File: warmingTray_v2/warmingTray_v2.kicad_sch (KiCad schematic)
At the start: 37 parts, among them J1 Jack-DC, P1 Power, P2 Analog, P3 Analog, P4 Digital, P5 PWM, P6 PWM, P7 Communication

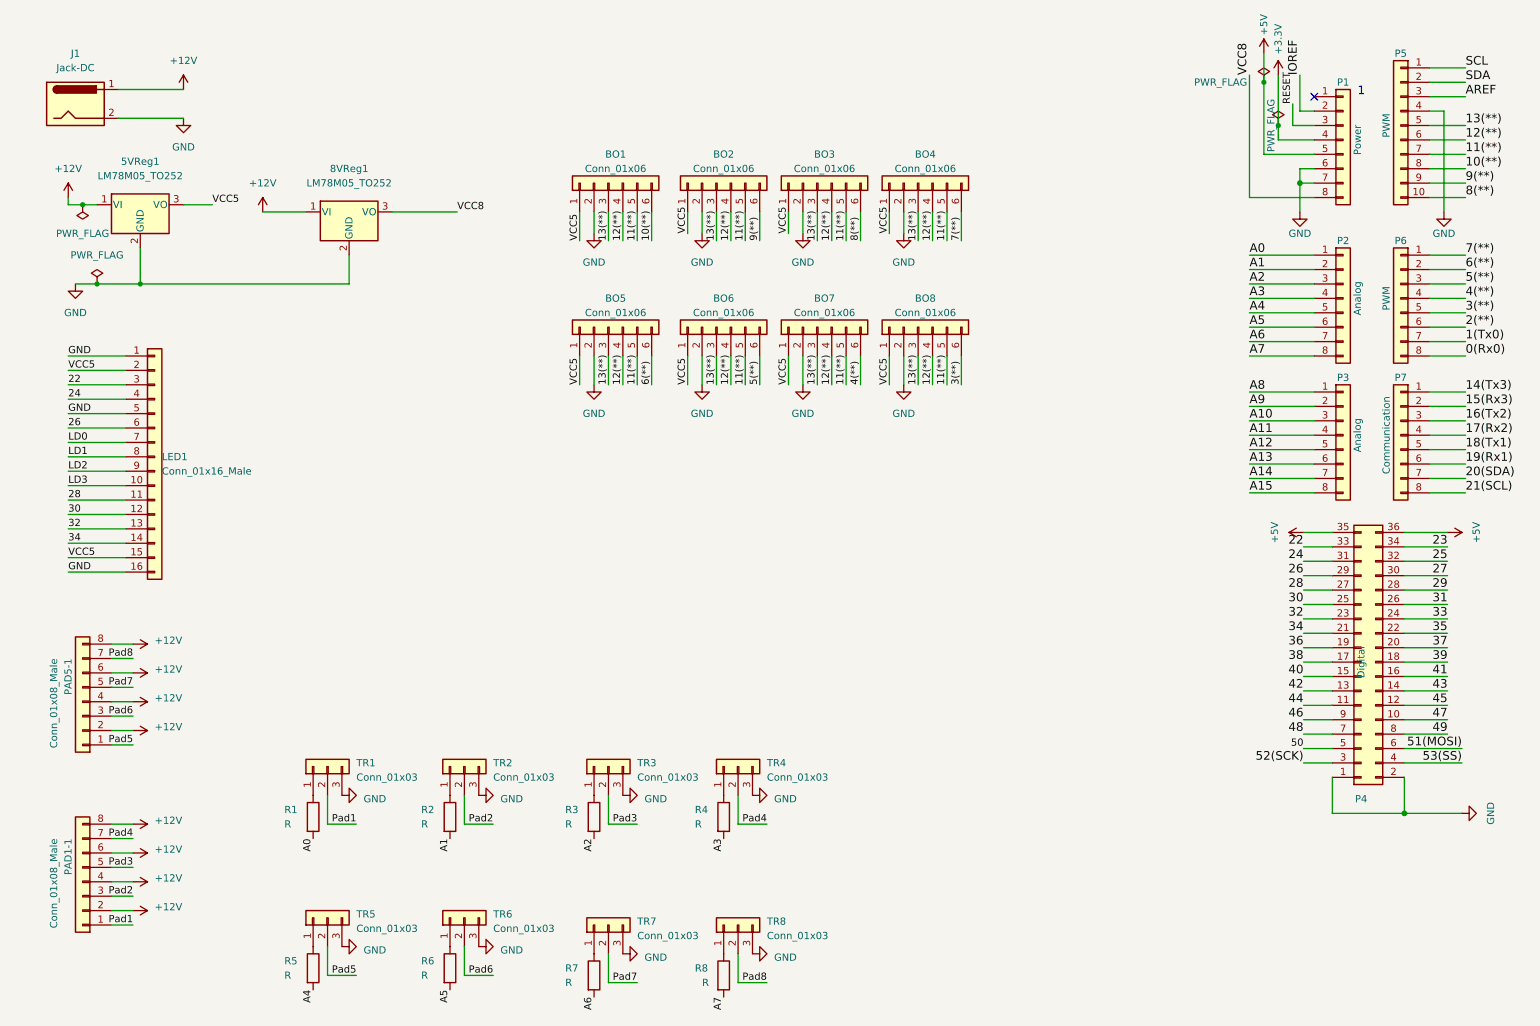
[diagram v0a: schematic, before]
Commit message: added traces to pcb
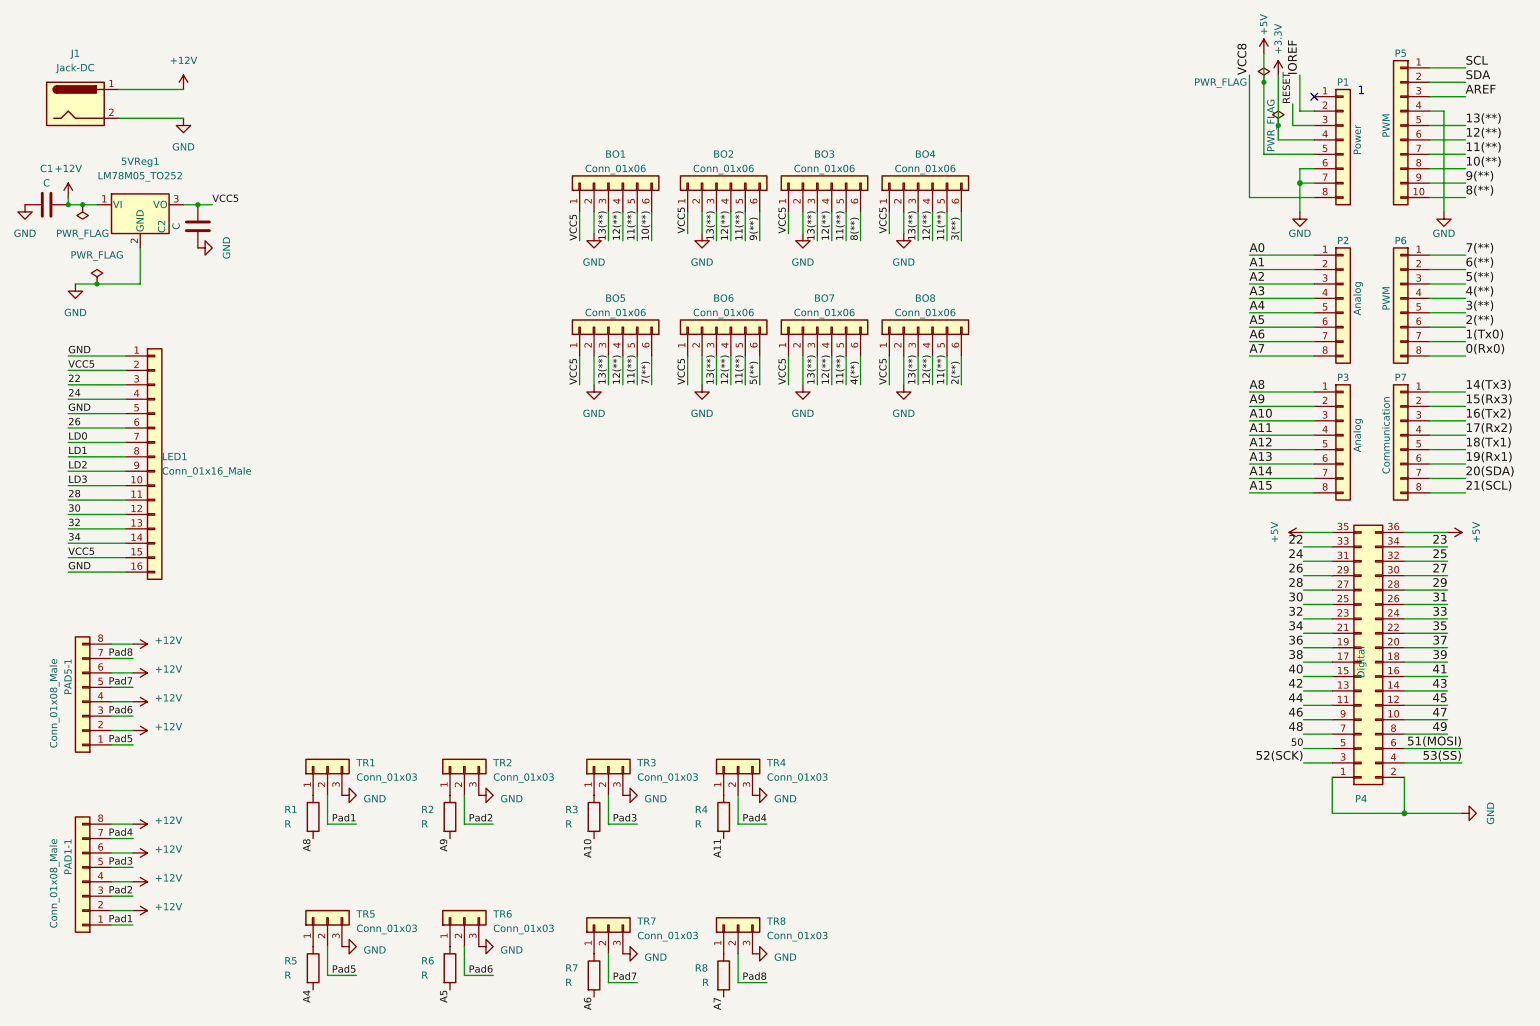
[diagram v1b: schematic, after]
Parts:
- removed 8VReg1: LM78M05_TO252, Package_TO_SOT_SMD:TO-252-2, symbol Regulator_Linear:LM78M05_TO252
- added C1: C, footprints_0-33uF:CAP_1608_TDK, symbol Device:C
- added C2: C, footprints_0-1uF_Capacitor:CAP_CL05_SAM, symbol Device:C
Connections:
- net +12V: now also C1.2
- net 2(**): now also BO8.6 (Pin_6)
- net 3(**): now also BO4.6 (Pin_6); no longer BO8.6 (Pin_6)
- net 6(**): no longer BO5.6 (Pin_6)
- net 7(**): now also BO5.6 (Pin_6); no longer BO4.6 (Pin_6)
- net A0: no longer R1.2
- net A1: no longer R2.2
- net A10: now also R3.2
- net A11: now also R4.2
- net A2: no longer R3.2
- net A3: no longer R4.2
- net A8: now also R1.2
- net A9: now also R2.2
- net GND: now also C1.1, C2.1
- net VCC5: now also C2.2
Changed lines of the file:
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@@
   (junction (at 240.03 43.18) (diameter 1.016) (color 0 0 0 0)
   )
-  (junction (at 35.56 60.96) (diameter 0) (color 0 0 0 0)
-  )
   (junction (at 25.4 46.99) (diameter 0) (color 0 0 0 0)
   )
@@
   (junction (at 258.445 154.305) (diameter 1.016) (color 0 0 0 0)
   )
+  (junction (at 22.86 46.99) (diameter 0) (color 0 0 0 0)
+  )
+  (junction (at 45.72 46.99) (diameter 0) (color 0 0 0 0)
+  )
   (junction (at 236.22 33.02) (diameter 0) (color 0 0 0 0)
   )
@@
     (stroke (width 0) (type solid))
   )
-  (wire (pts (xy 80.01 48.26) (xy 91.44 48.26))
-    (stroke (width 0) (type default))
-  )
   (wire (pts (xy 152.4 73.66) (xy 152.4 78.74))
     (stroke (width 0) (type default))
@@
     (stroke (width 0) (type solid))
   )
-  (wire (pts (xy 43.18 46.99) (xy 48.26 46.99))
+  (wire (pts (xy 43.18 46.99) (xy 45.72 46.99))
     (stroke (width 0) (type default))
   )
@@
     (stroke (width 0) (type solid))
   )
+  (wire (pts (xy 45.72 46.99) (xy 48.26 46.99))
+    (stroke (width 0) (type default))
+  )
   (wire (pts (xy 231.14 63.5) (xy 242.57 63.5))
     (stroke (width 0) (type solid))
@@
     (stroke (width 0) (type default))
   )
-  (wire (pts (xy 57.15 48.26) (xy 64.77 48.26))
-    (stroke (width 0) (type default))
-  )
   (wire (pts (xy 240.03 40.64) (xy 240.03 43.18))
     (stroke (width 0) (type solid))
@@
     (stroke (width 0) (type default))
   )
-  (wire (pts (xy 72.39 60.96) (xy 35.56 60.96))
-    (stroke (width 0) (type default))
-  )
   (wire (pts (xy 238.76 29.21) (xy 238.76 33.02))
     (stroke (width 0) (type default))
@@
     (stroke (width 0) (type solid))
   )
-  (wire (pts (xy 72.39 55.88) (xy 72.39 60.96))
-    (stroke (width 0) (type default))
-  )
   (wire (pts (xy 154.94 48.26) (xy 154.94 53.34))
     (stroke (width 0) (type default))
@@
     (effects (font (size 1.524 1.524)) (justify left bottom))
   )
-  (label "6(**)" (at 125.73 78.74 90) (fields_autoplaced)
+  (label "7(**)" (at 125.73 78.74 90) (fields_autoplaced)
     (effects (font (size 1.27 1.27)) (justify left bottom))
   )
@@
     (effects (font (size 1.524 1.524)) (justify right bottom))
   )
-  (label "3(**)" (at 180.34 78.74 90) (fields_autoplaced)
+  (label "2(**)" (at 180.34 78.74 90) (fields_autoplaced)
     (effects (font (size 1.27 1.27)) (justify left bottom))
   )
@@
     (effects (font (size 1.524 1.524)) (justify right bottom))
   )
-  (label "A0" (at 66.04 158.75 270) (fields_autoplaced)
+  (label "A8" (at 66.04 158.75 270) (fields_autoplaced)
     (effects (font (size 1.27 1.27)) (justify right bottom))
   )
@@
     (effects (font (size 1.27 1.27)) (justify right bottom))
   )
-  (label "7(**)" (at 180.34 53.34 90) (fields_autoplaced)
+  (label "3(**)" (at 180.34 53.34 90) (fields_autoplaced)
     (effects (font (size 1.27 1.27)) (justify left bottom))
   )
@@
     (effects (font (size 1.524 1.524)) (justify right bottom))
   )
-  (label "A1" (at 90.17 158.75 270) (fields_autoplaced)
+  (label "A9" (at 90.17 158.75 270) (fields_autoplaced)
     (effects (font (size 1.27 1.27)) (justify right bottom))
   )
@@
     (effects (font (size 1.524 1.524)) (justify left bottom))
   )
-  (label "A2" (at 115.57 158.75 270) (fields_autoplaced)
+  (label "A10" (at 115.57 158.75 270) (fields_autoplaced)
     (effects (font (size 1.27 1.27)) (justify right bottom))
   )
@@
     (effects (font (size 1.27 1.27)) (justify right bottom))
   )
-  (label "A3" (at 138.43 158.75 270) (fields_autoplaced)
+  (label "A11" (at 138.43 158.75 270) (fields_autoplaced)
     (effects (font (size 1.27 1.27)) (justify right bottom))
   )
@@
     (effects (font (size 1.27 1.27)) (justify left bottom))
   )
-  (label "VCC8" (at 91.44 48.26 0) (fields_autoplaced)
-    (effects (font (size 1.27 1.27)) (justify left bottom))
-  )
   (label "Pad3" (at 123.19 156.21 180) (fields_autoplaced)
     (effects (font (size 1.27 1.27)) (justify right bottom))
@@
     )
   )
+  (symbol (lib_id "Device:C") (at 19.05 46.99 90) (unit 1)
+    (in_bom yes) (on_board yes) (dnp no) (fields_autoplaced)
+    (property "Reference" "C1" (at 19.05 40.64 90)
+      (effects (font (size 1.27 1.27)))
+    )
+    (property "Value" "C" (at 19.05 43.18 90)
+      (effects (font (size 1.27 1.27)))
+    )
+    (property "Footprint" "footprints_0-33uF:CAP_1608_TDK" (at 22.86 46.0248 0)
+      (effects (font (size 1.27 1.27)) hide)
+    )
+    (property "Datasheet" "~" (at 19.05 46.99 0)
+      (effects (font (size 1.27 1.27)) hide)
+    )
+    (pin "1")
+    (pin "2")
+    (instances
+      (project "warmingTray_v2"
+        (path "/3761374c-22ef-4655-8f2e-3ccb2e58d193"
+          (reference "C1") (unit 1)
+        )
+      )
+    )
+  )
   (symbol (lib_id "Connector_Generic:Conn_01x08") (at 257.81 63.5 0) (mirror y) (unit 1)
     (in_bom yes) (on_board yes) (dnp no)
@@
     )
   )
+  (symbol (lib_id "Device:C") (at 45.72 50.8 180) (unit 1)
+    (in_bom yes) (on_board yes) (dnp no) (fields_autoplaced)
+    (property "Reference" "C2" (at 39.37 50.8 90)
+      (effects (font (size 1.27 1.27)))
+    )
+    (property "Value" "C" (at 41.91 50.8 90)
+      (effects (font (size 1.27 1.27)))
+    )
+    (property "Footprint" "footprints_0-1uF_Capacitor:CAP_CL05_SAM" (at 44.7548 46.99 0)
+      (effects (font (size 1.27 1.27)) hide)
+    )
+    (property "Datasheet" "~" (at 45.72 50.8 0)
+      (effects (font (size 1.27 1.27)) hide)
+    )
+    (pin "1")
+    (pin "2")
+    (instances
+      (project "warmingTray_v2"
+        (path "/3761374c-22ef-4655-8f2e-3ccb2e58d193"
+          (reference "C2") (unit 1)
+        )
+      )
+    )
+  )
   (symbol (lib_id "Connector_Generic:Conn_01x03") (at 118.11 173.99 90) (unit 1)
     (in_bom yes) (on_board yes) (dnp no) (fields_autoplaced)
@@
     )
   )
-  (symbol (lib_id "power:+12V") (at 57.15 48.26 0) (unit 1)
-    (in_bom yes) (on_board yes) (dnp no) (fields_autoplaced)
-    (property "Reference" "#PWR0117" (at 57.15 52.07 0)
-      (effects (font (size 1.27 1.27)) hide)
-    )
-    (property "Value" "+12V" (at 57.15 43.18 0)
-      (effects (font (size 1.27 1.27)))
-    )
-    (property "Footprint" "" (at 57.15 48.26 0)
-      (effects (font (size 1.27 1.27)) hide)
-    )
-    (property "Datasheet" "" (at 57.15 48.26 0)
-      (effects (font (size 1.27 1.27)) hide)
-    )
-    (pin "1")
-    (instances
-      (project "warmingTray_v2"
-        (path "/3761374c-22ef-4655-8f2e-3ccb2e58d193"
-          (reference "#PWR0117") (unit 1)
-        )
-      )
-    )
-  )
   (symbol (lib_id "Connector_Generic:Conn_01x06") (at 137.16 43.18 90) (unit 1)
     (in_bom yes) (on_board yes) (dnp no) (fields_autoplaced)
@@
     )
   )
-  (symbol (lib_id "Regulator_Linear:LM78M05_TO252") (at 72.39 48.26 0) (unit 1)
-    (in_bom yes) (on_board yes) (dnp no) (fields_autoplaced)
-    (property "Reference" "8VReg1" (at 72.39 40.64 0)
-      (effects (font (size 1.27 1.27)))
-    )
-    (property "Value" "LM78M05_TO252" (at 72.39 43.18 0)
-      (effects (font (size 1.27 1.27)))
-    )
-    (property "Footprint" "Package_TO_SOT_SMD:TO-252-2" (at 72.39 42.545 0)
-      (effects (font (size 1.27 1.27) italic) hide)
-    )
-    (property "Datasheet" "https://www.onsemi.com/pub/Collateral/MC78M00-D.PDF" (at 72.39 49.53 0)
-      (effects (font (size 1.27 1.27)) hide)
-    )
-    (pin "1")
-    (pin "2")
-    (pin "3")
-    (instances
-      (project "warmingTray_v2"
-        (path "/3761374c-22ef-4655-8f2e-3ccb2e58d193"
-          (reference "8VReg1") (unit 1)
-        )
-      )
-    )
-  )
   (symbol (lib_id "Connector:Jack-DC") (at 24.13 29.21 0) (unit 1)
     (in_bom yes) (on_board yes) (dnp no) (fields_autoplaced)
@@
     )
   )
+  (symbol (lib_id "power:GND") (at 45.72 54.61 90) (unit 1)
+    (in_bom yes) (on_board yes) (dnp no) (fields_autoplaced)
+    (property "Reference" "#PWR027" (at 52.07 54.61 0)
+      (effects (font (size 1.27 1.27)) hide)
+    )
+    (property "Value" "GND" (at 50.8 54.61 0)
+      (effects (font (size 1.27 1.27)))
+    )
+    (property "Footprint" "" (at 45.72 54.61 0)
+      (effects (font (size 1.27 1.27)) hide)
+    )
+    (property "Datasheet" "" (at 45.72 54.61 0)
+      (effects (font (size 1.27 1.27)) hide)
+    )
+    (pin "1")
+    (instances
+      (project "warmingTray_v2"
+        (path "/3761374c-22ef-4655-8f2e-3ccb2e58d193"
+          (reference "#PWR027") (unit 1)
+        )
+      )
+    )
+  )
   (symbol (lib_id "power:+5V") (at 266.065 104.775 270) (unit 1)
     (in_bom yes) (on_board yes) (dnp no) (fields_autoplaced)
@@
         )
       )
+    )
+  )
+  (symbol (lib_id "power:GND") (at 15.24 46.99 0) (unit 1)
+    (in_bom yes) (on_board yes) (dnp no) (fields_autoplaced)
+    (property "Reference" "#PWR026" (at 15.24 53.34 0)
+      (effects (font (size 1.27 1.27)) hide)
+    )
+    (property "Value" "GND" (at 15.24 52.07 0)
+      (effects (font (size 1.27 1.27)))
+    )
+    (property "Footprint" "" (at 15.24 46.99 0)
+      (effects (font (size 1.27 1.27)) hide)
+    )
+    (property "Datasheet" "" (at 15.24 46.99 0)
+      (effects (font (size 1.27 1.27)) hide)
+    )
+    (pin "1")
+    (instances
+      (project "warmingTray_v2"
+        (path "/3761374c-22ef-4655-8f2e-3ccb2e58d193"
+          (reference "#PWR026") (unit 1)
+        )
+      )

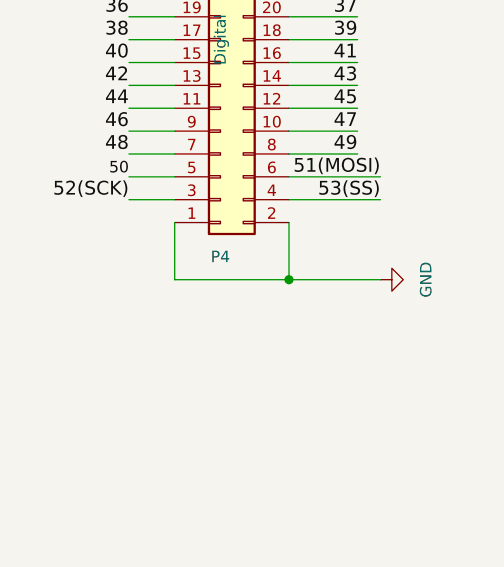
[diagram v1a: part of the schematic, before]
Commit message: PCB & Code
PCB: added 0805 footprints for resistors and capacitors
Code: testing controllers again so gains are being changed
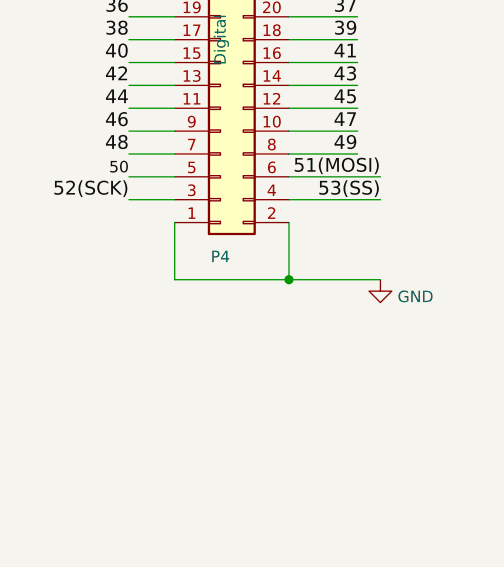
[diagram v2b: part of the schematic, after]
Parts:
- C1: footprint footprints_0-33uF:CAP_1608_TDK -> footprints_0805_0-33uF:CAP_CL21_SAM
- C2: footprint footprints_0-1uF_Capacitor:CAP_CL05_SAM -> footprints_0805_0-1uF:CAP_0805_B_WAL
- R1, R2, R3, R4, R5, R6, R7, R8: footprint footprints:RES_RK73G2A_KOA -> Resistor_SMD:R_0805_2012Metric_Pad1.20x1.40mm_HandSolder
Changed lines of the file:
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@@
       (effects (font (size 1.27 1.27)) (justify left))
     )
-    (property "Footprint" "footprints:RES_RK73G2A_KOA" (at 88.392 154.94 90)
+    (property "Footprint" "Resistor_SMD:R_0805_2012Metric_Pad1.20x1.40mm_HandSolder" (at 88.392 154.94 90)
       (effects (font (size 1.27 1.27)) hide)
     )
@@
       (effects (font (size 1.27 1.27)) (justify left))
     )
-    (property "Footprint" "footprints:RES_RK73G2A_KOA" (at 64.262 181.61 90)
+    (property "Footprint" "Resistor_SMD:R_0805_2012Metric_Pad1.20x1.40mm_HandSolder" (at 64.262 181.61 90)
       (effects (font (size 1.27 1.27)) hide)
     )
@@
       (effects (font (size 1.27 1.27)))
     )
-    (property "Footprint" "footprints_0-33uF:CAP_1608_TDK" (at 22.86 46.0248 0)
+    (property "Footprint" "footprints_0805_0-33uF:CAP_CL21_SAM" (at 22.86 46.0248 0)
       (effects (font (size 1.27 1.27)) hide)
     )
@@
       (effects (font (size 1.27 1.27)) (justify left))
     )
-    (property "Footprint" "footprints:RES_RK73G2A_KOA" (at 113.792 182.88 90)
+    (property "Footprint" "Resistor_SMD:R_0805_2012Metric_Pad1.20x1.40mm_HandSolder" (at 113.792 182.88 90)
       (effects (font (size 1.27 1.27)) hide)
     )
@@
       (effects (font (size 1.27 1.27)) (justify left))
     )
-    (property "Footprint" "footprints:RES_RK73G2A_KOA" (at 88.392 181.61 90)
+    (property "Footprint" "Resistor_SMD:R_0805_2012Metric_Pad1.20x1.40mm_HandSolder" (at 88.392 181.61 90)
       (effects (font (size 1.27 1.27)) hide)
     )
@@
     )
   )
-  (symbol (lib_id "power:GND") (at 268.605 154.305 90) (unit 1)
-    (in_bom yes) (on_board yes) (dnp no) (fields_autoplaced)
-    (property "Reference" "#PWR09" (at 274.955 154.305 0)
-      (effects (font (size 1.27 1.27)) hide)
-    )
-    (property "Value" "GND" (at 273.685 154.305 0)
-      (effects (font (size 1.27 1.27)))
+  (symbol (lib_id "power:GND") (at 268.605 154.305 0) (unit 1)
+    (in_bom yes) (on_board yes) (dnp no) (fields_autoplaced)
+    (property "Reference" "#PWR09" (at 268.605 160.655 0)
+      (effects (font (size 1.27 1.27)) hide)
+    )
+    (property "Value" "GND" (at 270.51 156.21 0)
+      (effects (font (size 1.27 1.27)) (justify left))
     )
     (property "Footprint" "" (at 268.605 154.305 0)
@@
       (effects (font (size 1.27 1.27)) (justify left))
     )
-    (property "Footprint" "footprints:RES_RK73G2A_KOA" (at 136.652 182.88 90)
+    (property "Footprint" "Resistor_SMD:R_0805_2012Metric_Pad1.20x1.40mm_HandSolder" (at 136.652 182.88 90)
       (effects (font (size 1.27 1.27)) hide)
     )
@@
       (effects (font (size 1.27 1.27)))
     )
-    (property "Footprint" "footprints_0-1uF_Capacitor:CAP_CL05_SAM" (at 44.7548 46.99 0)
+    (property "Footprint" "footprints_0805_0-1uF:CAP_0805_B_WAL" (at 44.7548 46.99 0)
       (effects (font (size 1.27 1.27)) hide)
     )
@@
       (effects (font (size 1.27 1.27)) (justify left))
     )
-    (property "Footprint" "footprints:RES_RK73G2A_KOA" (at 64.262 154.94 90)
+    (property "Footprint" "Resistor_SMD:R_0805_2012Metric_Pad1.20x1.40mm_HandSolder" (at 64.262 154.94 90)
       (effects (font (size 1.27 1.27)) hide)
     )
@@
       (effects (font (size 1.27 1.27)) (justify left))
     )
-    (property "Footprint" "footprints:RES_RK73G2A_KOA" (at 136.652 154.94 90)
+    (property "Footprint" "Resistor_SMD:R_0805_2012Metric_Pad1.20x1.40mm_HandSolder" (at 136.652 154.94 90)
       (effects (font (size 1.27 1.27)) hide)
     )
@@
       (effects (font (size 1.27 1.27)) (justify left))
     )
-    (property "Footprint" "footprints:RES_RK73G2A_KOA" (at 113.792 154.94 90)
-      (effects (font (size 1.27 1.27)) hide)
-    )
+    (property "Footprint" "Resistor_SMD:R_0805_2012Metric_Pad1.20x1.40mm_HandSolder" (at 113.792 154.94 90)
+      (effects (font (size 1.27 1.27)) hide)
+    )
